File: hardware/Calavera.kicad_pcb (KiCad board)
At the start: 2 copper layers, 39.2 x 59.2 mm, 24 parts, among them Q1 Q_DUAL_NMOS, U1 AT42QT1012, U2 LMV932

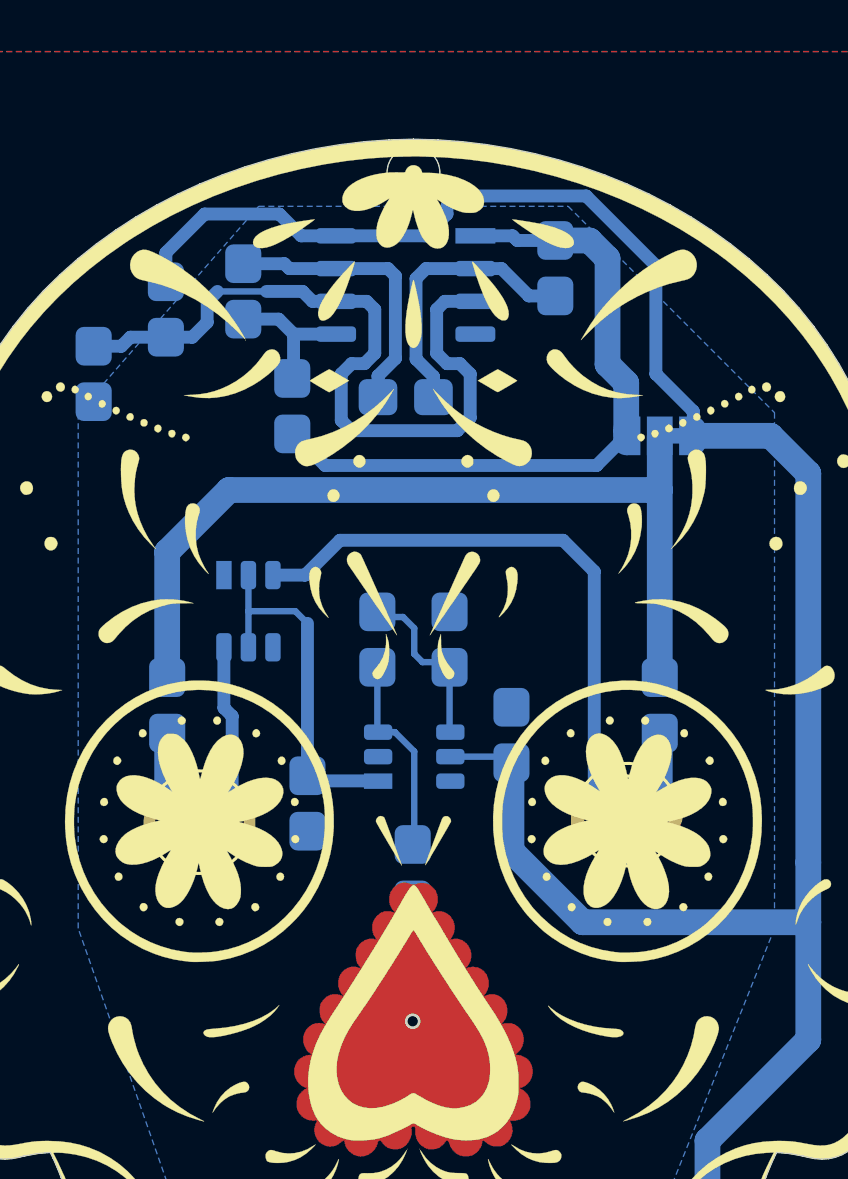
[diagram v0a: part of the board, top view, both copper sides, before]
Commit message: Updated To KiCad6
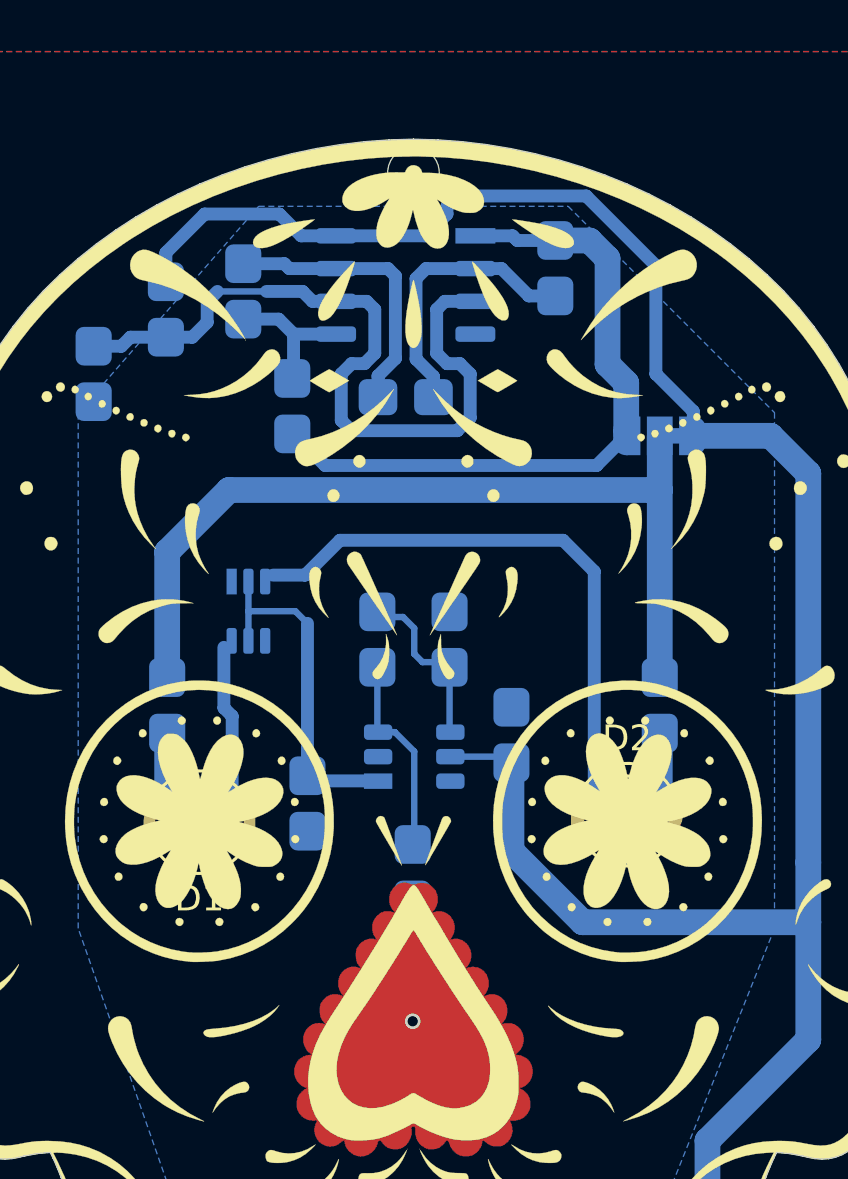
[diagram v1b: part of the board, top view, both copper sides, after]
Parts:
- added H1: Ø2mm, Calavera:MountingHole_2mm, F.Cu at (139.2, 74.5)
- D1, D2: footprint LED_THT:LED_D3.0mm -> Calavera:LED_D3.0mm_ThroughHole
- G1: footprint Calavera:Cap_Pad -> Calavera:Calavera_Cap_Pad
- JP1: footprint Jumper:SolderJumper-3_P1.3mm_Bridged12_RoundedPad1.0x1.5mm -> Calavera:SolderJumper-3_P1.3mm_Bridged12_RoundedPad1.0x1.5mm
- Q1: footprint Calavera:SOT23-6-NMOSx2_Handsolder -> Calavera:SOT-363_NX138BKS_Handsolder
- U1: footprint Calavera:SOT23-6-AT42QT1012 -> Calavera:SOT23-6-AT42QT1012_Handsolder
- U2: footprint Calavera:SOIC-8_Dual_OpAmp -> Calavera:SOIC-8_Dual_OpAmp_Handsolder
- renumbered R6 to R4, R4 to R5, R5 to R6
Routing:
- net (no net): vias 1 -> 0
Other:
- net class Default removed

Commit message: v0.3.0 see changelog for details
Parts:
- added SW1: SW_SPDT, Calavera:Slider_Switch_C&K_AYZ0102AGRLC_SPDT_RightAngle, B.Cu at (152.1, 107.9)
- BT1: footprint Calavera:CR2032_Multicomp_MP000357_Alternative -> Calavera:CR2032_Keystone_3024
- Q1: value Q_DUAL_NMOS -> DMN65D8L; footprint Calavera:SOT-363_NX138BKS_Handsolder -> Calavera:SOT-23_NMOS_DMN65D8L
- moved Q1 1.36 mm to (134.1, 91.9), turned to 180 degrees
- moved C3 0.91 mm to (144.8, 79.1)
- moved R10 0.41 mm to (126.7, 81.9)
- moved R8 0.40 mm to (132.6, 79.5)
- moved R3 0.25 mm to (135.1, 99.2)
- moved R9 0.14 mm to (129.7, 79.7)
- moved U1 0.05 mm to (139.2, 97.1)
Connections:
- BT1 pad +: VCC -> Net-(BT1-Pad+)
- D1 pad 1: VLEDK1 -> VLEDK
- D2 pad 1: VLEDK2 -> VLEDK
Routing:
- net VCC: track 124.7 -> 78.7 mm
- net VLEDK: track 0.00 -> 34.6 mm
- net VLEDK2: track 23.0 -> 0.00 mm
- net Net-(BT1-Pad+): track 0.00 -> 11.1 mm
- net VLEDK1: track 6.91 -> 0.00 mm
- net Cap_Out: track 13.6 -> 7.66 mm
- net Vbias: track 29.7 -> 29.0 mm
- net Net-(C3-Pad1): track 10.9 -> 11.5 mm
- net VLED: track 34.7 -> 35.3 mm
- net Net-(R4-Pad2): track 11.1 -> 10.6 mm
- net GND: vias 0 -> 2
- added copper zone on F.Cu, net GND
- removed copper zone on B.Cu, net (none)
- removed copper zone on F.Cu, net (none)

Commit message: Cap touch area is bigger. Added some vias to connect both planes
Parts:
- moved G1 3.75 mm to (139.2, 106.5)
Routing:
- net GND: vias 2 -> 12

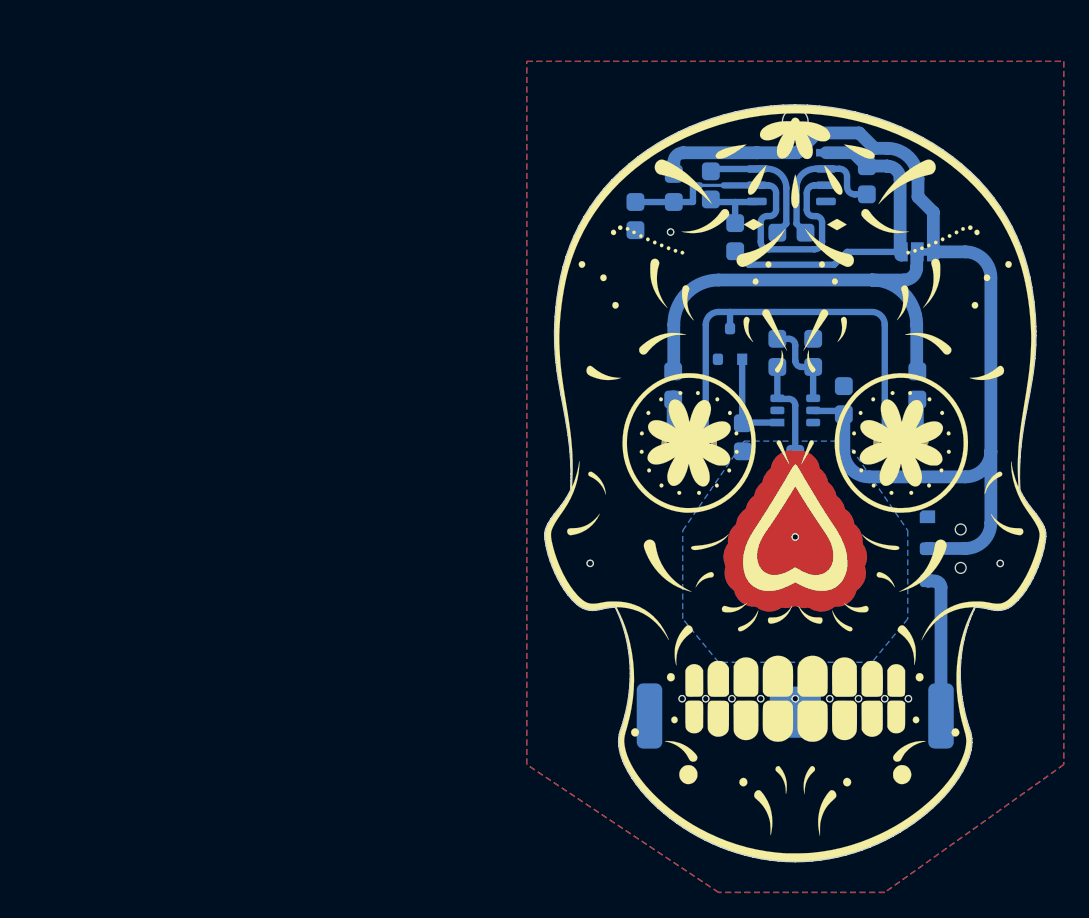
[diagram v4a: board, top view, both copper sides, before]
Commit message: Small edit of the Art. Small changes here and there to account for new DRCs in KiCad 7
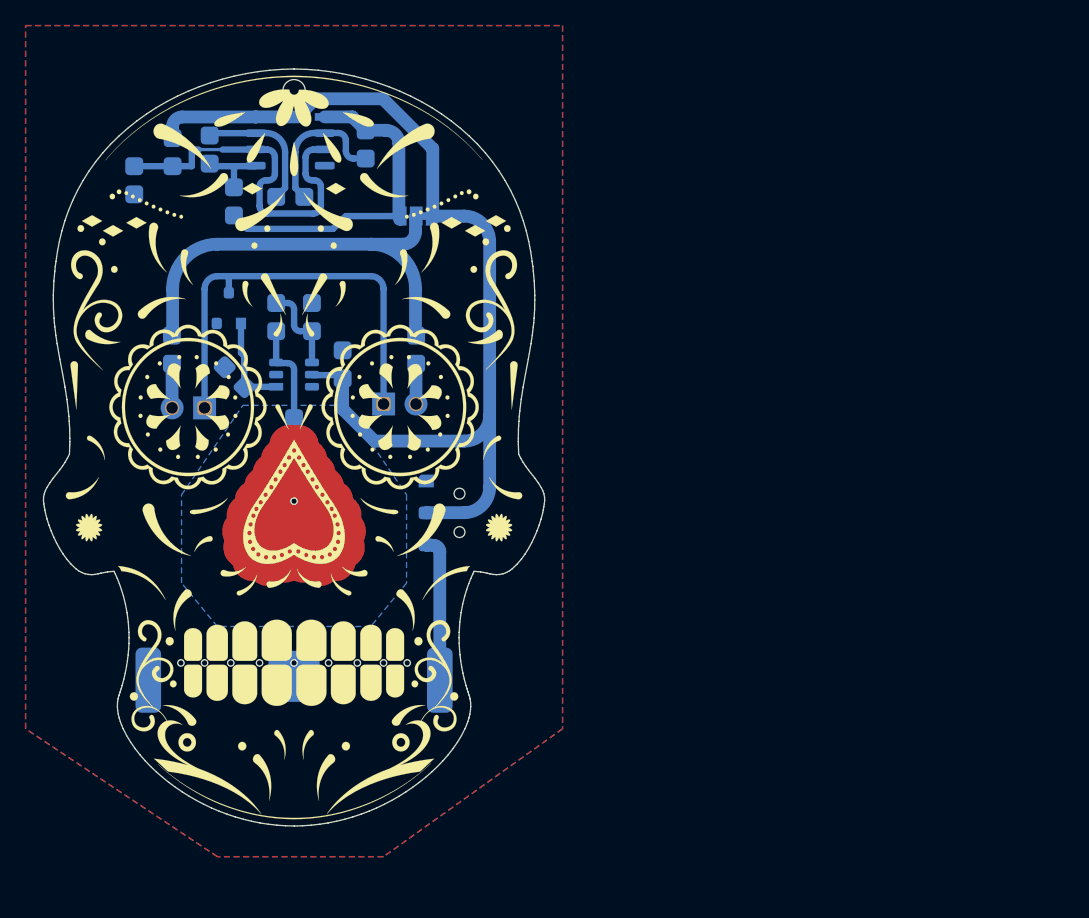
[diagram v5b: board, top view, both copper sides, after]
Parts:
- removed G2: Edge, Calavera:Calavera_Board_Margins
- removed G3: Mask, Calavera:Calavera_SolderMask_1200dpi_Border
- removed G4: Silk, Calavera:Calavera_SilkScreen_1200dpi
- G1: value HeartPad -> Calavera_Art; footprint Calavera:Calavera_Cap_Pad -> Calavera:Calavera_Art
- H1: footprint Calavera:MountingHole_2mm -> Calavera:MountingHole_1.75mm
- R5, R6: value R_Small_US -> RΩ
- U1: footprint Calavera:SOT23-6-AT42QT1012_Handsolder -> Calavera:SOT23-6-AT42QT1012
- moved R3 40.0 mm to (95.3, 94.5), turned to 135 degrees
- moved G1 39.7 mm to (100.0, 100.0)
- moved D2 39.3 mm to (107.0, 96.6)
- moved C1 39.3 mm to (98.6, 89.8)
- moved C3 39.3 mm to (105.6, 76.3)
- moved C2 39.3 mm to (103.8, 93.5)
- moved JP1 39.3 mm to (109.5, 81.9)
- moved R10 39.3 mm to (87.5, 79.1)
- moved R4 39.3 mm to (99.7, 80.4)
- moved R5 39.3 mm to (90.5, 92.3)
- moved R6 39.3 mm to (109.5, 92.3)
- moved R7 39.3 mm to (95.3, 80.8)
- moved U2 39.3 mm to (99.7, 76.0)
- moved BT1 39.3 mm to (100.0, 117.9)
- moved Q1 39.3 mm to (94.9, 89.1)
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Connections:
- net /Sense renamed CapTouch
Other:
- rule pad_to_mask_clearance: 0.1 -> 0

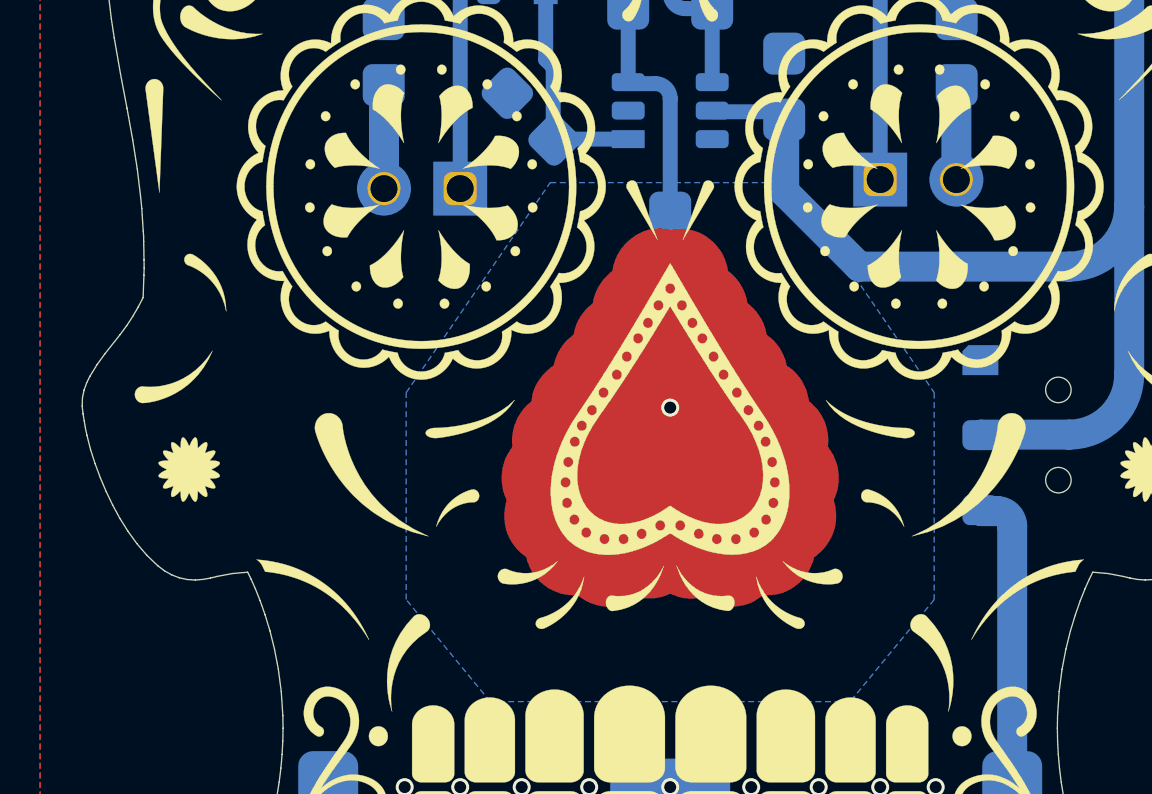
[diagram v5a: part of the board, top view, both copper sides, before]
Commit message: Hand tweaks to the art to avoid most of the ERC errors
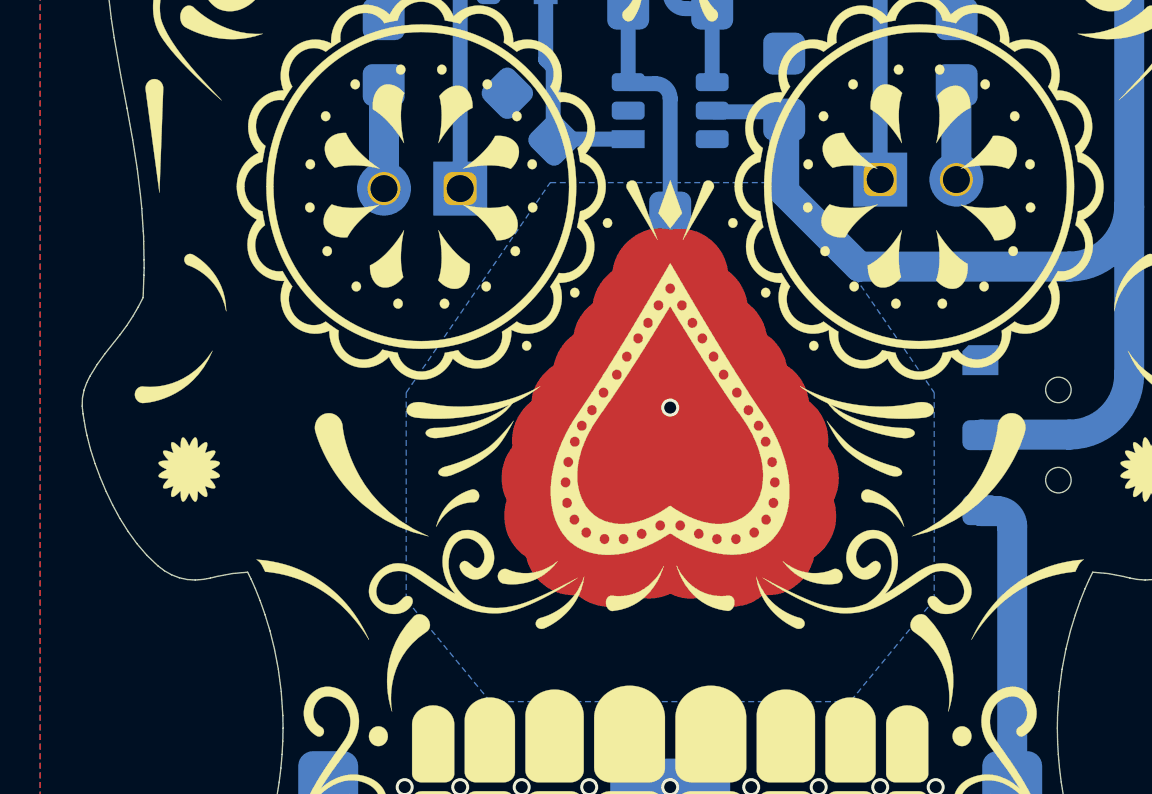
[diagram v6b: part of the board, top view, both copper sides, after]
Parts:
- H1: value Ø2mm -> Ø1.75mm
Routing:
- net GND: vias 12 -> 11

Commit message: Tweaks on the project for KiBot
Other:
- outline, holes or cut-outs redrawn
- board text removed: "IMPORT NETLIST =========== Importint the netlist shows two warnings for the copper plane. I wanted to leave them unconnected, so they will have to stay, I guess"
